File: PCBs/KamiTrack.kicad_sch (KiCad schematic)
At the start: 63 parts, among them J1 Conn_01x02_Female, J2 Conn_01x04_Female, J3 Conn_01x02_Female, J4 Conn_01x08_Female, J5 Conn_01x02_Female, P1 USB_C_Plug_USB2.0, SW1 Option/FLASH Switch, SW2 Cali Switch, SW3 SW_SPDT MAIN POWER, U1 ME6211C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

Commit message: Added sheet description
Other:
- company: (none) -> github.com/Kamilake/KamiTrack-SlimeVR-PCB
- title: (none) -> KamiTrack-SlimeVR-PCB
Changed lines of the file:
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@@
 (kicad_sch (version 20211123) (generator eeschema)
   (paper "A4")
+  (title_block
+    (title "KamiTrack-SlimeVR-PCB")
+    (date "2022-04-07")
+    (rev "v0.4")
+    (company "github.com/Kamilake/KamiTrack-SlimeVR-PCB")
+    (comment 1 "Licensed under CERN-OHL-P v2 or later")
+    (comment 2 "Compatible with github.com/SlimeVR/SlimeVR-Tracker-ESP")
+  )
   (junction (at 50.8 158.75) (diameter 0) (color 0 0 0 0)
   )
@@
     (stroke (width 0) (type default) (color 0 0 0 0))
   )
+  (wire (pts (xy 95.25 121.92) (xy 104.14 121.92))
+    (stroke (width 0) (type default) (color 0 0 0 0))
+  )
   (wire (pts (xy 199.39 53.34) (xy 196.85 53.34))
     (stroke (width 0) (type default) (color 0 0 0 0))
@@
     )
   )
-  (global_label "ADC" (shape input) (at 104.14 121.92 180) (fields_autoplaced)
-    (effects (font (size 1.27 1.27)) (justify right))
-    (property "Intersheet References" "${INTERSHEET_REFS}" (id 0) (at 0 0 0)
-      (effects (font (size 1.27 1.27)) hide)
-    )
+  (global_label "ADC" (shape input) (at 95.25 121.92 180) (fields_autoplaced)
+    (effects (font (size 1.27 1.27)) (justify right))
+    (property "Intersheet References" "${INTERSHEET_REFS}" (id 0) (at -8.89 0 0)
+      (effects (font (size 1.27 1.27)) hide)
+    )

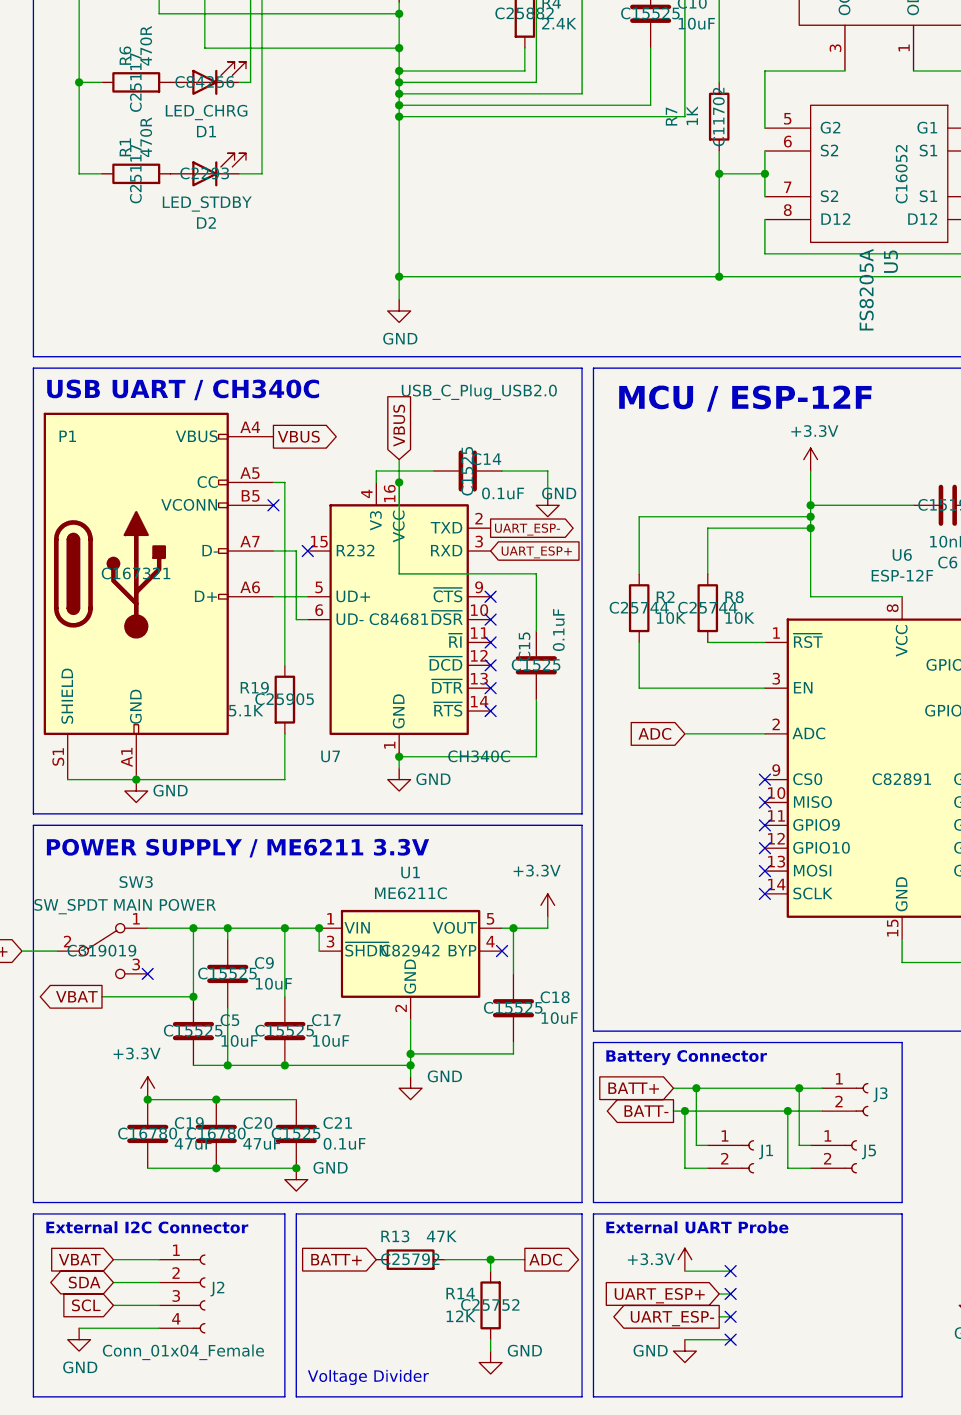
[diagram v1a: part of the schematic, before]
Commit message: Standby LED Change to C34499
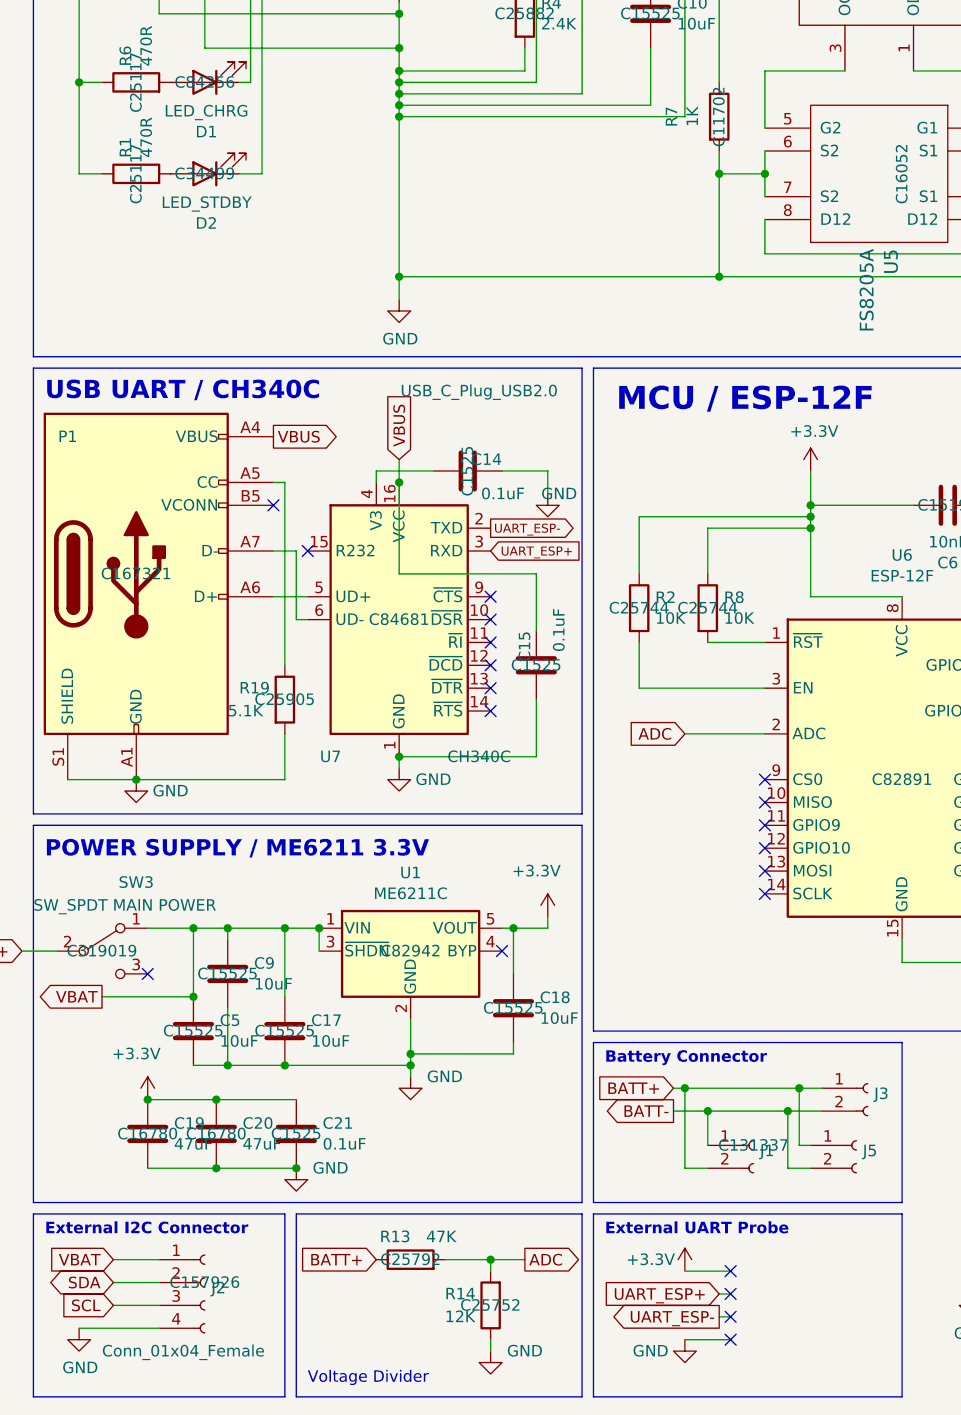
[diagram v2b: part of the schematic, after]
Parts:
- D2: LCSC C2293 -> C34499
- J1: footprint Connector_JST:JST_PH_S2B-PH-K_1x02_P2.00mm_Horizontal -> Connector_JST:JST_PH_B2B-PH-K_1x02_P2.00mm_Vertical; LCSC (none) -> C131337
- J2: LCSC (none) -> C157926
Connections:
- net BATT+: now also J1.2 (Pin_2); no longer J1.1 (Pin_1)
- net BATT-: now also J1.1 (Pin_1); no longer J1.2 (Pin_2)
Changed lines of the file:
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@@
   (junction (at 63.5 71.12) (diameter 0) (color 0 0 0 0)
   )
-  (junction (at 95.25 163.83) (diameter 0) (color 0 0 0 0)
-  )
   (junction (at 34.29 127) (diameter 0) (color 0 0 0 0)
   )
@@
   (junction (at 63.5 124.46) (diameter 0) (color 0 0 0 0)
   )
-  (junction (at 96.52 161.29) (diameter 0) (color 0 0 0 0)
+  (junction (at 95.25 161.29) (diameter 0) (color 0 0 0 0)
   )
   (junction (at 196.85 85.09) (diameter 0) (color 0 0 0 0)
@@
   (junction (at 109.22 99.06) (diameter 0) (color 0 0 0 0)
   )
+  (junction (at 97.79 163.83) (diameter 0) (color 0 0 0 0)
+  )
   (junction (at 251.46 148.59) (diameter 0) (color 0 0 0 0)
   )
@@
     (stroke (width 0) (type default) (color 0 0 0 0))
   )
-  (wire (pts (xy 96.52 161.29) (xy 107.95 161.29))
+  (wire (pts (xy 93.98 161.29) (xy 95.25 161.29))
     (stroke (width 0) (type default) (color 0 0 0 0))
   )
@@
     (stroke (width 0) (type default) (color 0 0 0 0))
   )
-  (wire (pts (xy 95.25 170.18) (xy 97.79 170.18))
-    (stroke (width 0) (type default) (color 0 0 0 0))
-  )
   (wire (pts (xy 227.33 40.64) (xy 196.85 40.64))
     (stroke (width 0) (type default) (color 0 0 0 0))
@@
     (stroke (width 0) (type default) (color 0 0 0 0))
   )
-  (wire (pts (xy 93.98 163.83) (xy 95.25 163.83))
-    (stroke (width 0) (type default) (color 0 0 0 0))
-  )
   (wire (pts (xy 227.33 53.34) (xy 237.49 53.34))
     (stroke (width 0) (type default) (color 0 0 0 0))
@@
     (stroke (width 0) (type default) (color 0 0 0 0))
   )
+  (wire (pts (xy 97.79 163.83) (xy 106.68 163.83))
+    (stroke (width 0) (type default) (color 0 0 0 0))
+  )
   (wire (pts (xy 199.39 81.28) (xy 196.85 81.28))
     (stroke (width 0) (type default) (color 0 0 0 0))
@@
     (stroke (width 0) (type default) (color 0 0 0 0))
   )
-  (wire (pts (xy 95.25 163.83) (xy 106.68 163.83))
+  (wire (pts (xy 93.98 163.83) (xy 97.79 163.83))
     (stroke (width 0) (type default) (color 0 0 0 0))
   )
@@
     (stroke (width 0) (type default) (color 0 0 0 0))
   )
+  (wire (pts (xy 95.25 161.29) (xy 95.25 170.18))
+    (stroke (width 0) (type default) (color 0 0 0 0))
+  )
   (wire (pts (xy 63.5 49.53) (xy 78.74 49.53))
     (stroke (width 0) (type default) (color 0 0 0 0))
@@
     (stroke (width 0) (type default) (color 0 0 0 0))
   )
-  (wire (pts (xy 93.98 161.29) (xy 96.52 161.29))
-    (stroke (width 0) (type default) (color 0 0 0 0))
-  )
   (wire (pts (xy 129.54 68.58) (xy 129.54 64.77))
     (stroke (width 0) (type default) (color 0 0 0 0))
@@
     (stroke (width 0) (type default) (color 0 0 0 0))
   )
+  (wire (pts (xy 97.79 163.83) (xy 97.79 167.64))
+    (stroke (width 0) (type default) (color 0 0 0 0))
+  )
   (wire (pts (xy 190.5 85.09) (xy 196.85 85.09))
     (stroke (width 0) (type default) (color 0 0 0 0))
@@
     (stroke (width 0) (type default) (color 0 0 0 0))
   )
+  (wire (pts (xy 95.25 161.29) (xy 107.95 161.29))
+    (stroke (width 0) (type default) (color 0 0 0 0))
+  )
   (wire (pts (xy 148.59 144.78) (xy 148.59 147.32))
     (stroke (width 0) (type default) (color 0 0 0 0))
   )
+  (wire (pts (xy 95.25 170.18) (xy 97.79 170.18))
+    (stroke (width 0) (type default) (color 0 0 0 0))
+  )
   (wire (pts (xy 198.12 133.35) (xy 204.47 133.35))
     (stroke (width 0) (type default) (color 0 0 0 0))
@@
     (stroke (width 0) (type default) (color 0 0 0 0))
   )
-  (wire (pts (xy 97.79 167.64) (xy 96.52 167.64))
-    (stroke (width 0) (type default) (color 0 0 0 0))
-  )
   (wire (pts (xy 99.06 71.12) (xy 167.64 71.12))
     (stroke (width 0) (type default) (color 0 0 0 0))
@@
     (stroke (width 0) (type default) (color 0 0 0 0))
   )
-  (wire (pts (xy 96.52 167.64) (xy 96.52 161.29))
-    (stroke (width 0) (type default) (color 0 0 0 0))
-  )
   (wire (pts (xy 49.53 106.68) (xy 53.34 106.68))
     (stroke (width 0) (type default) (color 0 0 0 0))
@@
     (stroke (width 0) (type default) (color 0 0 0 0))
   )
-  (wire (pts (xy 95.25 170.18) (xy 95.25 163.83))
-    (stroke (width 0) (type default) (color 0 0 0 0))
-  )
   (wire (pts (xy 171.45 38.1) (xy 171.45 45.72))
     (stroke (width 0) (type default) (color 0 0 0 0))
@@
       (effects (font (size 1.27 1.27)) hide)
     )
-    (property "LCSC" "C2293" (id 4) (at 41.91 59.69 0))
+    (property "LCSC" "C34499" (id 4) (at 41.91 59.69 0))
     (pin "1")
     (pin "2")
@@
       (effects (font (size 1.27 1.27)) (justify left) hide)
     )
-    (property "Footprint" "Connector_JST:JST_PH_S2B-PH-K_1x02_P2.00mm_Horizontal" (id 2) (at 102.87 167.64 0)
+    (property "Footprint" "Connector_JST:JST_PH_B2B-PH-K_1x02_P2.00mm_Vertical" (id 2) (at 102.87 167.64 0)
       (effects (font (size 1.27 1.27)) hide)
     )
@@
       (effects (font (size 1.27 1.27)) hide)
     )
+    (property "LCSC" "C131337" (id 4) (at 102.87 167.64 0))
     (pin "1")
     (pin "2")
@@
       (effects (font (size 1.27 1.27)) hide)
     )
+    (property "LCSC" "C157926" (id 4) (at 41.91 182.88 0))
     (pin "1")
     (pin "2")
@@
     )
     (path "/00000000-0000-0000-0000-000061f07241"
-      (reference "J1") (unit 1) (value "Conn_01x02_Female") (footprint "Connector_JST:JST_PH_S2B-PH-K_1x02_P2.00mm_Horizontal")
+      (reference "J1") (unit 1) (value "Conn_01x02_Female") (footprint "Connector_JST:JST_PH_B2B-PH-K_1x02_P2.00mm_Vertical")
     )
     (path "/00000000-0000-0000-0000-000062288446"

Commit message: JLCPCB_CORRECTION
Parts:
- U2, U3, U6, U7, U8: JLCPCB_CORRECTION (none) -> 0;0;270
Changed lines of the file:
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@@
     )
     (property "LCSC" "C24112" (id 4) (at 231.14 130.81 0))
+    (property "JLCPCB_CORRECTION" "0;0;270" (id 5) (at 231.14 133.35 0))
     (pin "1")
     (pin "10")
@@
       (effects (font (size 1.524 1.524)))
     )
-    (property "LCSC" "C16581" (id 4) (at 63.5 30.48 0))
+    (property "LCSC" "C16581" (id 4) (at 63.5 26.67 0))
+    (property "JLCPCB_CORRECTION" "0;0;270" (id 5) (at 63.5 29.21 0))
     (pin "1")
     (pin "2")
@@
     )
     (property "LCSC" "C82891" (id 4) (at 119.38 127 0))
+    (property "JLCPCB_CORRECTION" "0;0;270" (id 5) (at 119.38 129.54 0))
     (pin "1")
     (pin "10")
@@
       (effects (font (size 1.27 1.27)) hide)
     )
-    (property "LCSC" "C84681" (id 4) (at 63.5 109.22 0))
+    (property "LCSC" "C84681" (id 4) (at 62.23 111.76 0))
+    (property "JLCPCB_CORRECTION" "0;0;270" (id 5) (at 62.23 114.3 0))
     (pin "1")
     (pin "10")
@@
     )
     (property "LCSC" "C976032" (id 4) (at 212.09 68.58 0))
+    (property "JLCPCB_CORRECTION" "0;0;270" (id 5) (at 212.09 71.12 0))
     (pin "1")
     (pin "10")

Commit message: add JLCPCB_CORRECTION
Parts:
- J1: footprint Connector_JST:JST_PH_B2B-PH-K_1x02_P2.00mm_Vertical -> Connector_JST:JST_PH_S2B-PH-K_1x02_P2.00mm_Horizontal; JLCPCB_CORRECTION (none) -> 0;0;180; LCSC C131337 -> C173752
- J3: LCSC (none) -> C173752
- P1, U1, U4: JLCPCB_CORRECTION (none) -> 0;0;180
- U5: JLCPCB_CORRECTION (none) -> 0;0;270
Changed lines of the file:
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@@
       (effects (font (size 1.524 1.524)) hide)
     )
-    (property "LCSC" "C181096" (id 4) (at 116.84 36.83 0))
+    (property "LCSC" "C181096" (id 4) (at 116.84 35.56 0))
+    (property "JLCPCB_CORRECTION" "0;0;180" (id 5) (at 116.84 38.1 0))
     (pin "1")
     (pin "2")
@@
       (effects (font (size 1.524 1.524)) hide)
     )
-    (property "LCSC" "C16052" (id 4) (at 119.38 59.69 0))
+    (property "LCSC" "C16052" (id 4) (at 116.84 59.69 0))
+    (property "JLCPCB_CORRECTION" "0;0;270" (id 5) (at 119.38 59.69 0))
     (pin "1")
     (pin "2")
@@
       (effects (font (size 1.27 1.27)) (justify left) hide)
     )
-    (property "Footprint" "Connector_JST:JST_PH_B2B-PH-K_1x02_P2.00mm_Vertical" (id 2) (at 102.87 167.64 0)
+    (property "Footprint" "Connector_JST:JST_PH_S2B-PH-K_1x02_P2.00mm_Horizontal" (id 2) (at 102.87 167.64 0)
       (effects (font (size 1.27 1.27)) hide)
     )
@@
       (effects (font (size 1.27 1.27)) hide)
     )
-    (property "LCSC" "C131337" (id 4) (at 102.87 167.64 0))
+    (property "LCSC" "C173752" (id 4) (at 100.33 172.72 0))
+    (property "JLCPCB_CORRECTION" "0;0;180" (id 5) (at 109.22 172.72 0))
     (pin "1")
     (pin "2")
@@
       (effects (font (size 1.27 1.27)) hide)
     )
+    (property "LCSC" "C173752" (id 4) (at 114.3 165.1 0))
     (pin "1")
     (pin "2")
@@
     )
     (property "LCSC" "C167321" (id 4) (at 34.29 104.14 0))
+    (property "JLCPCB_CORRECTION" "0;0;180" (id 5) (at 34.29 104.14 0)
+      (effects (font (size 1.27 1.27)) hide)
+    )
     (pin "A1")
     (pin "A12")
@@
     )
     (property "LCSC" "C82942" (id 4) (at 64.77 146.05 0))
+    (property "JLCPCB_CORRECTION" "0;0;180" (id 5) (at 64.77 146.05 0)
+      (effects (font (size 1.27 1.27)) hide)
+    )
     (pin "1")
     (pin "2")
@@
     )
     (path "/00000000-0000-0000-0000-000061f07241"
-      (reference "J1") (unit 1) (value "Conn_01x02_Female") (footprint "Connector_JST:JST_PH_B2B-PH-K_1x02_P2.00mm_Vertical")
+      (reference "J1") (unit 1) (value "Conn_01x02_Female") (footprint "Connector_JST:JST_PH_S2B-PH-K_1x02_P2.00mm_Horizontal")
     )
     (path "/00000000-0000-0000-0000-000062288446"

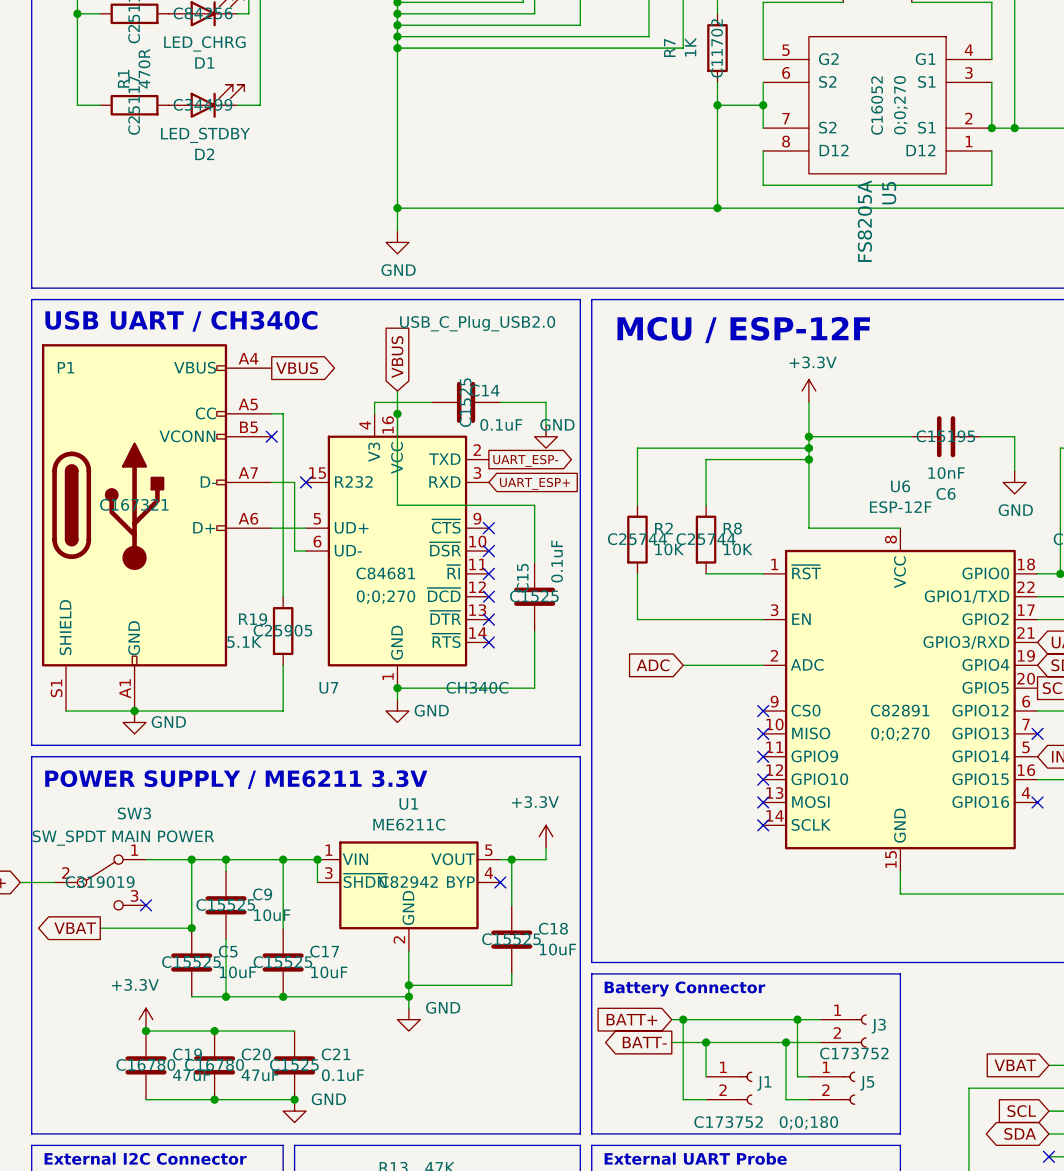
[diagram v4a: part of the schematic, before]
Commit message: add more JLCPCB_CORRECTION
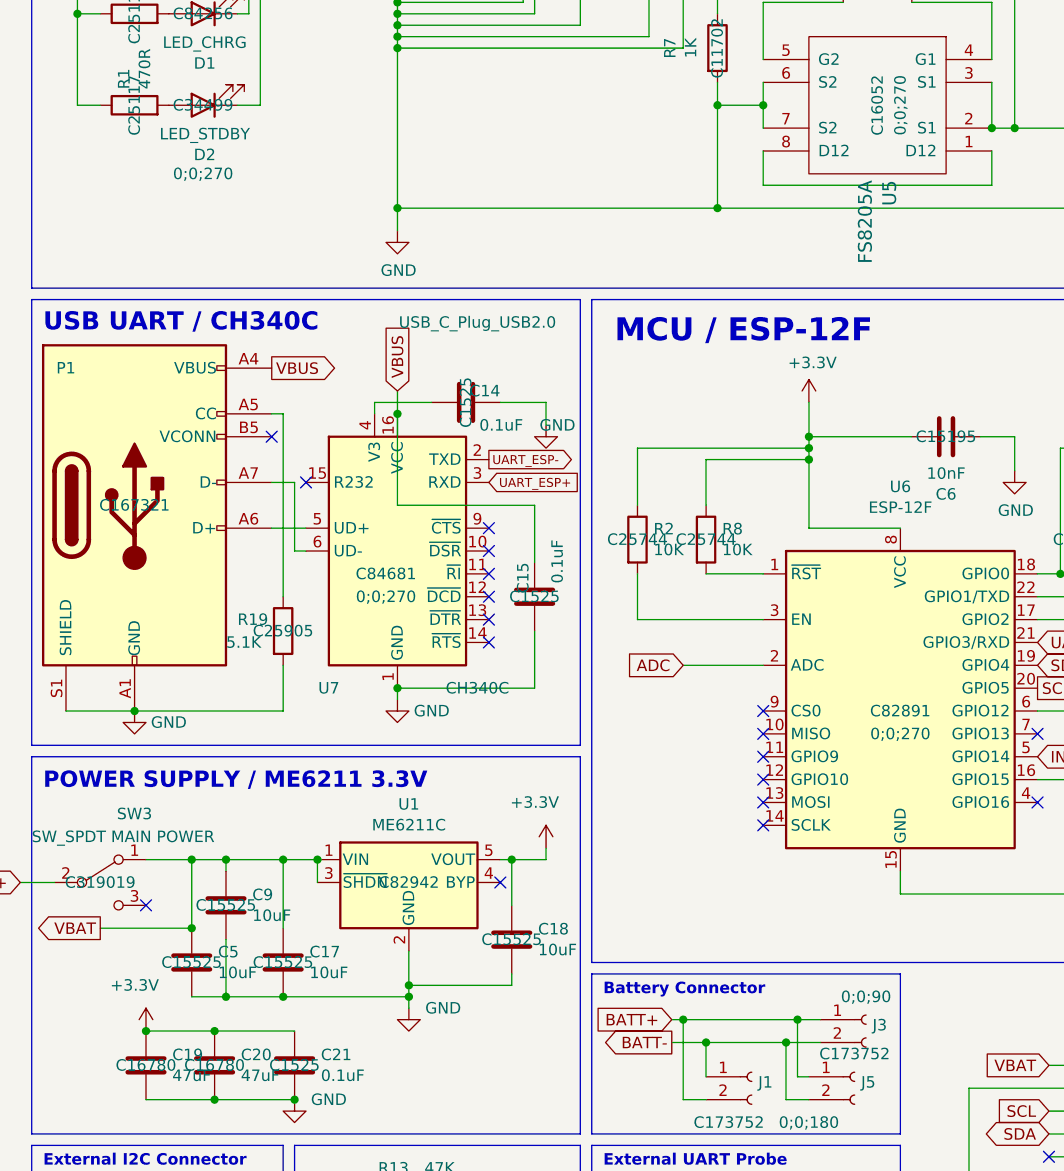
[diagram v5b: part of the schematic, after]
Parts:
- D2: JLCPCB_CORRECTION (none) -> 0;0;270
- J3: JLCPCB_CORRECTION (none) -> 0;0;90
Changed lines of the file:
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@@
     )
     (property "LCSC" "C34499" (id 4) (at 41.91 59.69 0))
+    (property "JLCPCB_CORRECTION" "0;0;270" (id 5) (at 41.91 67.31 0))
     (pin "1")
     (pin "2")
@@
     )
     (property "LCSC" "C173752" (id 4) (at 114.3 165.1 0))
-    (pin "1")
-    (pin "2")
+    (property "JLCPCB_CORRECTION" "0;0;90" (id 5) (at 115.57 158.75 0))
+    (pin "1")
+    (pin "2")

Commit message: JLCPCB_CORRECTION;;;;;;;;;;;
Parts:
- D2: JLCPCB_CORRECTION 0;0;270 -> 0;0;0
- J3: JLCPCB_CORRECTION 0;0;90 -> 0;0;0
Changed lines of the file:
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@@
     )
     (property "LCSC" "C34499" (id 4) (at 41.91 59.69 0))
-    (property "JLCPCB_CORRECTION" "0;0;270" (id 5) (at 41.91 67.31 0))
+    (property "JLCPCB_CORRECTION" "0;0;0" (id 5) (at 41.91 67.31 0))
     (pin "1")
     (pin "2")
@@
     )
     (property "LCSC" "C173752" (id 4) (at 114.3 165.1 0))
-    (property "JLCPCB_CORRECTION" "0;0;90" (id 5) (at 115.57 158.75 0))
-    (pin "1")
-    (pin "2")
+    (property "JLCPCB_CORRECTION" "0;0;0" (id 5) (at 115.57 158.75 0))
+    (pin "1")
+    (pin "2")
